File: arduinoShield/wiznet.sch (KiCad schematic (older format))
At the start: 54 parts

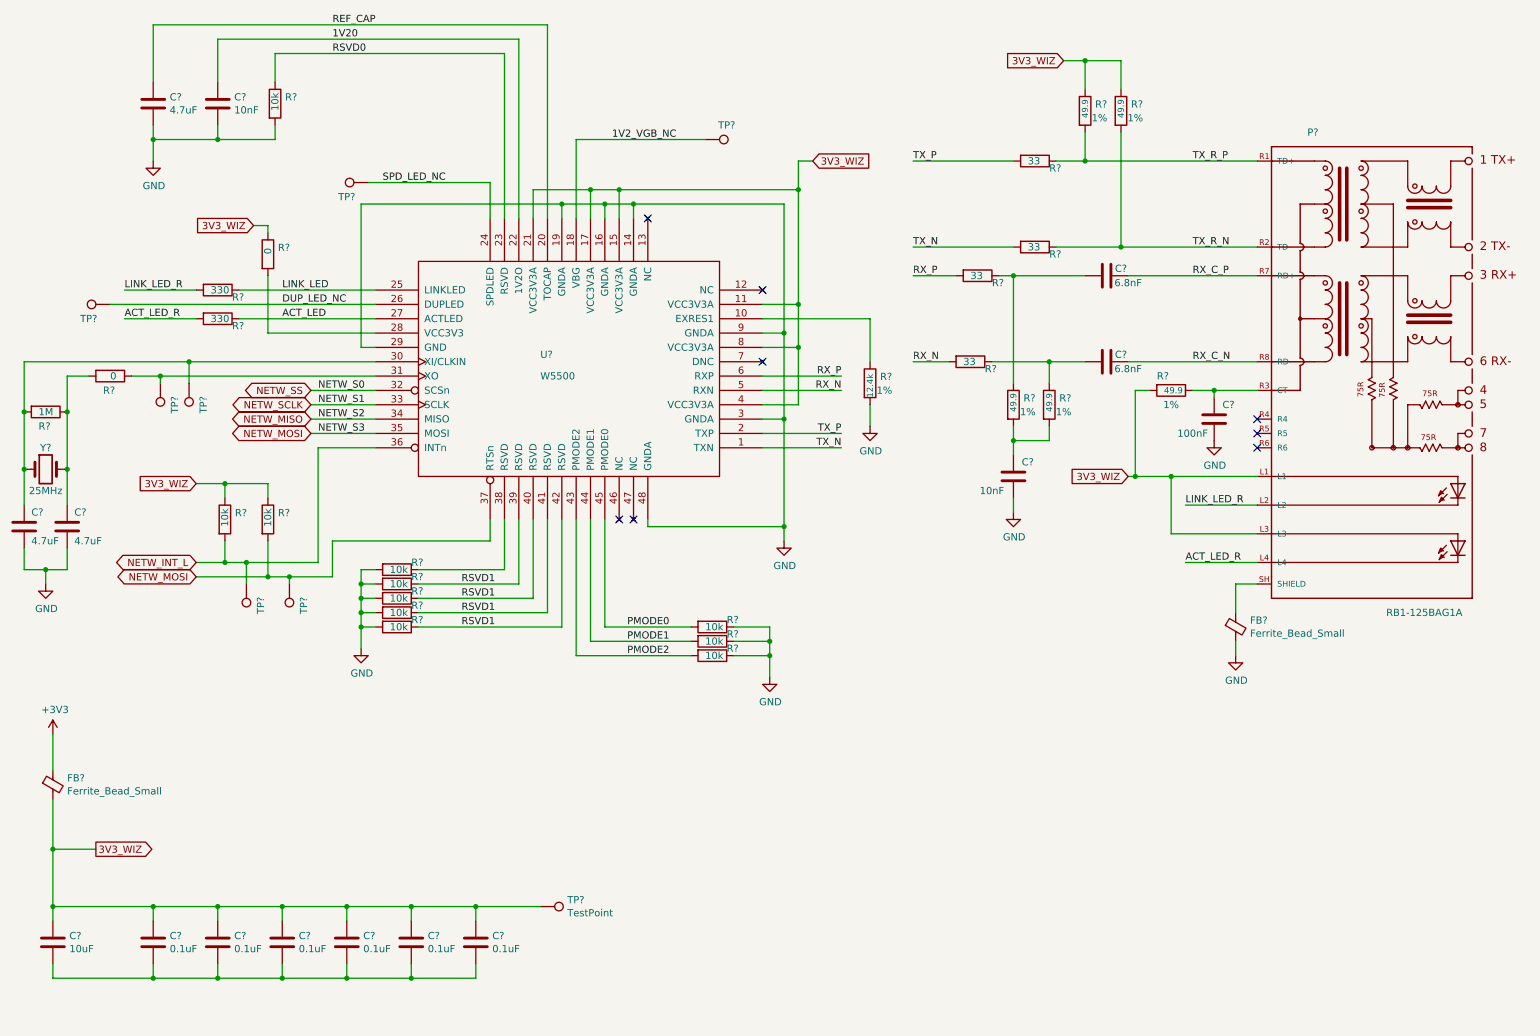
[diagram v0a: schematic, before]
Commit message: Added sensors
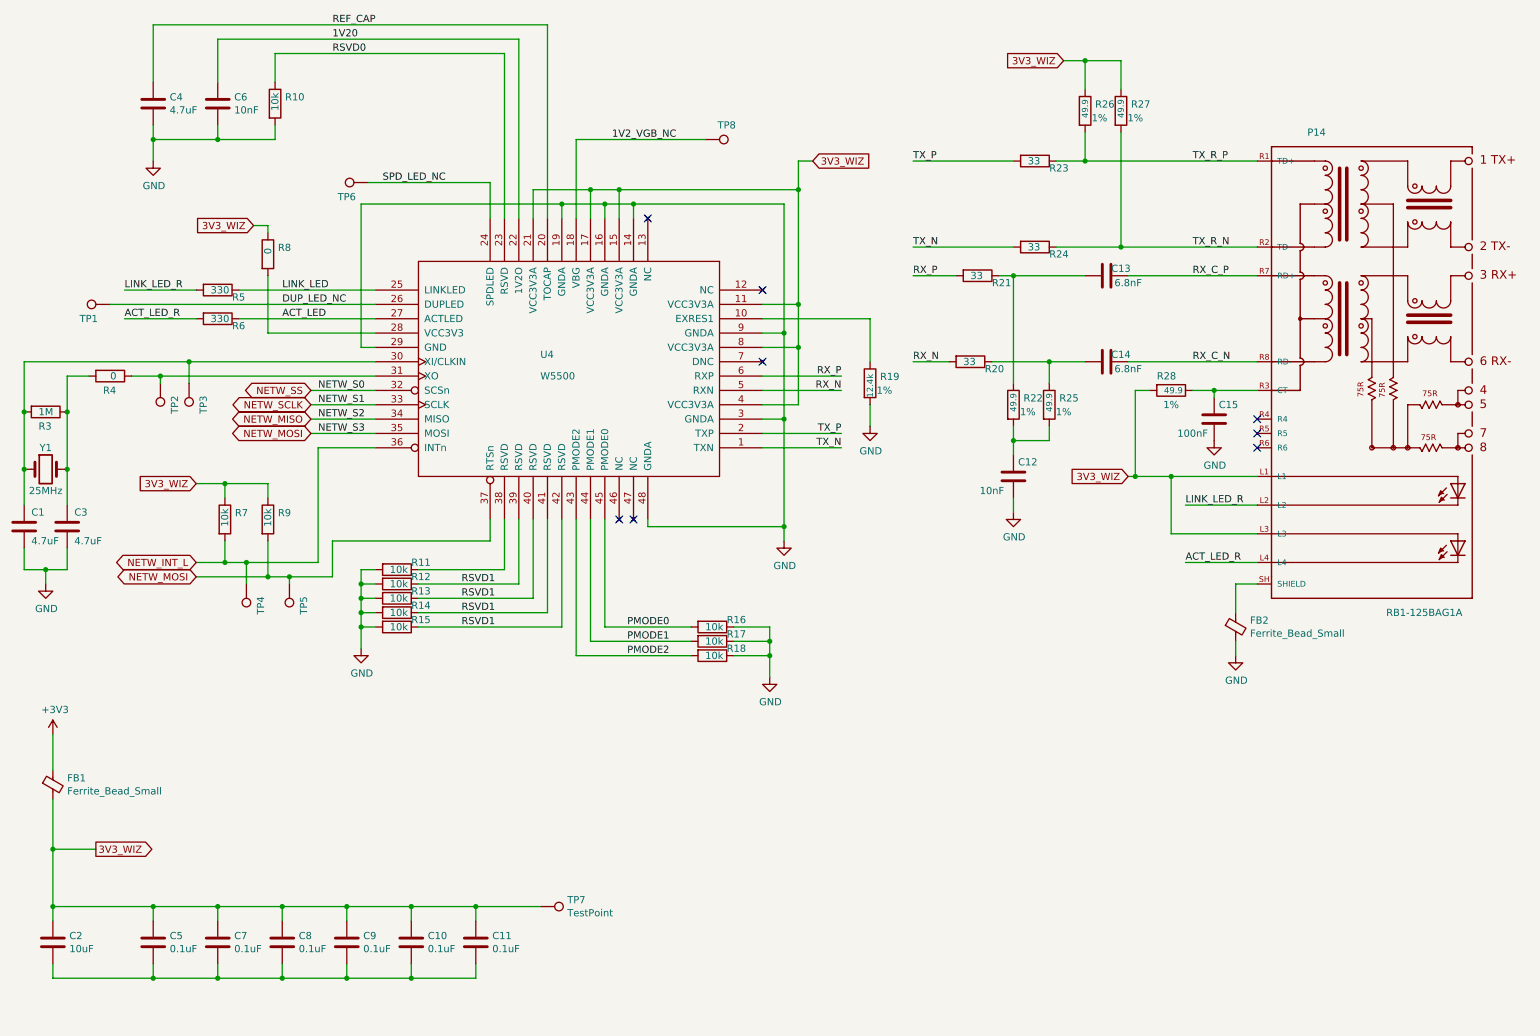
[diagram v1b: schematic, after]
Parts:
- gave numbers to parts that had none: 54

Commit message: Starting layout
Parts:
- P14: footprint WIZNET_RB1-125BAG1A -> footprints:WIZNET_RB1-125BAG1A
- U4: footprint MODULE -> footprints:QFP50P900X900X160-48N
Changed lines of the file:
@@
 F 0 "U4" H 4700 3000 50  0000 R CNN
 F 1 "W5500" H 4700 3150 50  0000 R CNN
-F 2 "MODULE" H 4500 3100 50  0001 C CNN
-F 3 "DOCUMENTATION" H 4500 3100 50  0001 C CNN
+F 2 "footprints:QFP50P900X900X160-48N" H 4500 3100 50  0001 C CNN
+F 3 "http://wizwiki.net/wiki/lib/exe/fetch.php?media=products:w5500:w5500_ds_v106e_141230.pdf" H 4500 3100 50  0001 C CNN
 	1    4500 3100
 	-1   0    0    1
@@
 F 0 "P14" H 9650 4650 50  0000 L CNN
 F 1 "RB1-125BAG1A" H 10200 1300 50  0000 L CNN
-F 2 "WIZNET_RB1-125BAG1A" H 10100 3050 50  0001 L BNN
+F 2 "footprints:WIZNET_RB1-125BAG1A" H 10100 3050 50  0001 L BNN
 F 3 "2.18 USD" H 10100 3050 50  0001 L BNN
 F 4 "Good" H 10100 3050 50  0001 L BNN "Availability"

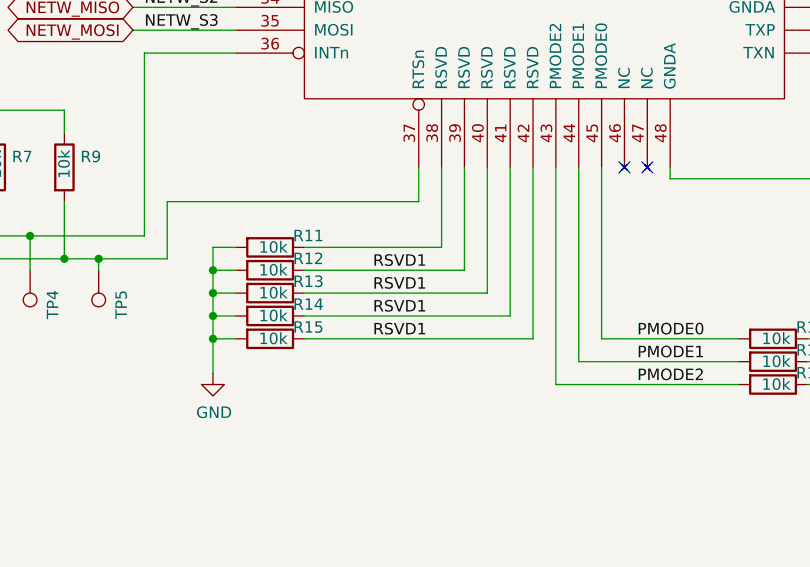
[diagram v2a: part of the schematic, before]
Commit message: Half of wiznet is layed out. Fixed PMODE termination resistors.
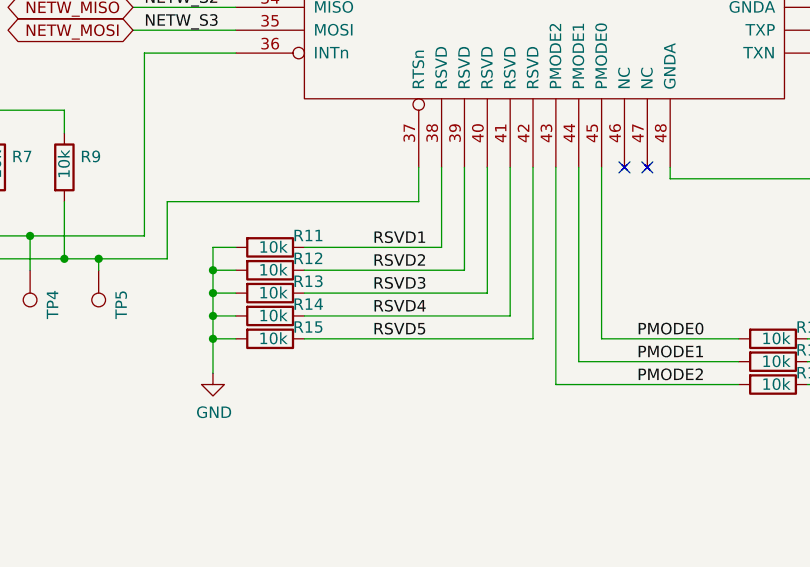
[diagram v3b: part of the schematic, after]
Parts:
- R16, R17, R18: footprint Resistors_SMD:R_0402 -> Resistors_SMD:R_0805
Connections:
- net RSVD1: now also R11.1, U4.38 (RSVD); no longer R12.1, R13.1, R14.1, R15.1, U4.39 (RSVD), U4.40 (RSVD), U4.41 (RSVD), U4.42 (RSVD)
- new net RSVD2: R12.1, U4.39 (RSVD)
- new net RSVD3: R13.1, U4.40 (RSVD)
- new net RSVD4: R14.1, U4.41 (RSVD)
- new net RSVD5: R15.1, U4.42 (RSVD)
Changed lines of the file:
@@
 Text Label 5200 4900 2    50   ~ 0
 PMODE0
+Text Label 3750 4500 0    50   ~ 0
+RSVD1
 Text Label 3750 4600 0    50   ~ 0
-RSVD1
+RSVD2
 Text Label 3750 4700 0    50   ~ 0
-RSVD1
+RSVD3
 Text Label 3750 4800 0    50   ~ 0
-RSVD1
-Text Label 3750 4900 0    50   ~ 0
-RSVD1
+RSVD4
 Wire Wire Line
 	700  3050 1850 3050
@@
 F 0 "R16" V 5450 5000 50  0000 L CNN
 F 1 "10k" V 5500 4850 50  0000 L CNN
-F 2 "Resistors_SMD:R_0402" V 5430 4900 50  0001 C CNN
+F 2 "Resistors_SMD:R_0805" V 5430 4900 50  0001 C CNN
 F 3 "~" H 5500 4900 50  0001 C CNN
 	1    5500 4900
@@
 F 0 "R17" V 5450 5100 50  0000 L CNN
 F 1 "10k" V 5500 4950 50  0000 L CNN
-F 2 "Resistors_SMD:R_0402" V 5430 5000 50  0001 C CNN
+F 2 "Resistors_SMD:R_0805" V 5430 5000 50  0001 C CNN
 F 3 "~" H 5500 5000 50  0001 C CNN
 	1    5500 5000
@@
 F 0 "R18" V 5450 5200 50  0000 L CNN
 F 1 "10k" V 5500 5050 50  0000 L CNN
-F 2 "Resistors_SMD:R_0402" V 5430 5100 50  0001 C CNN
+F 2 "Resistors_SMD:R_0805" V 5430 5100 50  0001 C CNN
 F 3 "~" H 5500 5100 50  0001 C CNN
 	1    5500 5100
@@
 Text Label 8850 3050 0    50   ~ 0
 RX_C_N
+Text Label 3750 4900 0    50   ~ 0
+RSVD5
 $EndSCHEMATC

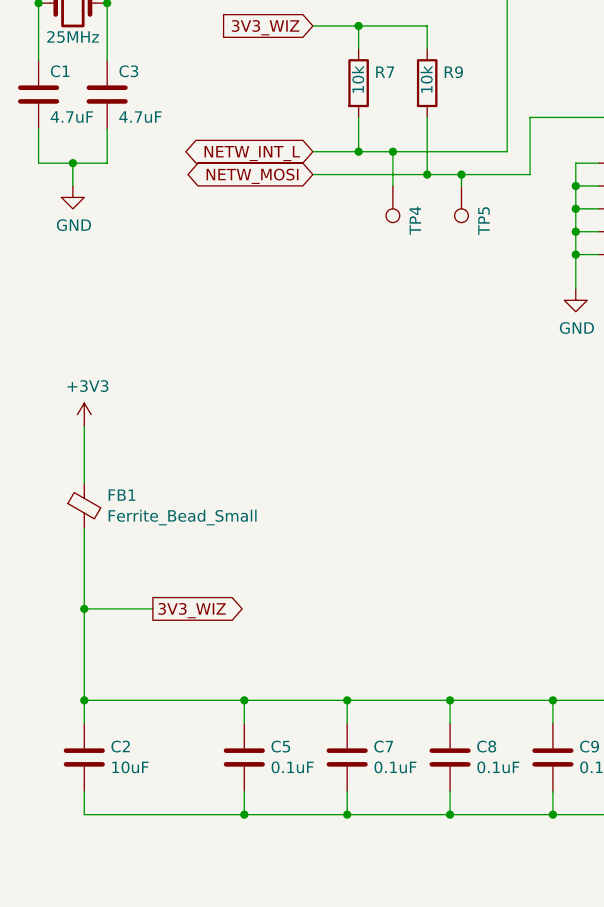
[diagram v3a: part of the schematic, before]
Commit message: Inital layout done. Starting routing. Need to add breakout headers for analogue.
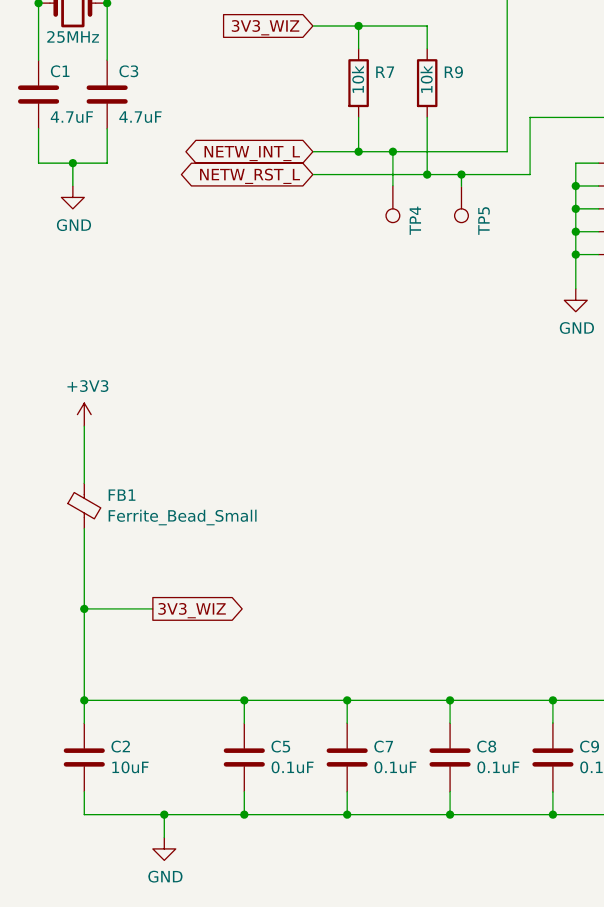
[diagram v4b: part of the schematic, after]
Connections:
- net GND: now also C10.2, C11.2, C2.2, C5.2, C7.2, C8.2, C9.2
- net NETW_MOSI: no longer R9.2, TP5.1, U4.37 (RTSn)
- new net NETW_RST_L: R9.2, TP5.1, U4.37 (RTSn)
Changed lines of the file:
@@
 	3400 7350 3850 7350
 Wire Wire Line
-	1600 7350 900  7350
+	1600 7350 1250 7350
 Wire Wire Line
 	900  7350 900  7250
@@
 NETW_INT_L
 Text GLabel 1900 4550 0    50   BiDi ~ 0
-NETW_MOSI
+NETW_RST_L
 $Comp
 L Device:R R7
@@
 Text Label 3750 4900 0    50   ~ 0
 RSVD5
+$Comp
+L power:GND #PWR?
+U 1 1 5CF3217B
+P 1250 7450
+F 0 "#PWR?" H 1250 7200 50  0001 C CNN
+F 1 "GND" H 1255 7277 50  0000 C CNN
+F 2 "" H 1250 7450 50  0001 C CNN
+F 3 "" H 1250 7450 50  0001 C CNN
+	1    1250 7450
+	1    0    0    -1
+$EndComp
+Connection ~ 1250 7350
+Wire Wire Line
+	1250 7350 900  7350
+Wire Wire Line
+	1250 7450 1250 7350
 $EndSCHEMATC

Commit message: Power planes created. Started routing.
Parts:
- FB1: footprint Resistors_SMD:R_0402 -> Resistors_SMD:R_1206
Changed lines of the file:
@@
 F 0 "FB1" H 1000 6046 50  0000 L CNN
 F 1 "Ferrite_Bead_Small" H 1000 5955 50  0000 L CNN
-F 2 "Resistors_SMD:R_0402" V 830 6000 50  0001 C CNN
+F 2 "Resistors_SMD:R_1206" V 830 6000 50  0001 C CNN
 F 3 "~" H 900 6000 50  0001 C CNN
 	1    900  6000
@@
 RSVD5
 $Comp
-L power:GND #PWR?
+L power:GND #PWR0118
 U 1 1 5CF3217B
 P 1250 7450
-F 0 "#PWR?" H 1250 7200 50  0001 C CNN
+F 0 "#PWR0118" H 1250 7200 50  0001 C CNN
 F 1 "GND" H 1255 7277 50  0000 C CNN
 F 2 "" H 1250 7450 50  0001 C CNN

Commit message: Made slack changes from review
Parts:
- added R38, R39, R40: 0, Resistors_SMD:R_0402, symbol Device:R
- P14: symbol hyper_capstone:RB1-125BAG1A -> arduinoShield-rescue:RB1-125BAG1A-hyper_capstone
- U4: symbol hyper_capstone:W5500 -> arduinoShield-rescue:W5500-hyper_capstone
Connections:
- net NETW_MOSI: now also R40.2; no longer U4.35 (MOSI)
- net NETW_SCLK: now also R39.2; no longer U4.33 (SCLK)
- net NETW_SS: now also R38.2; no longer U4.32 (SCSn)
- new net NETW_S0: R38.1, U4.32 (SCSn)
- new net NETW_S1: R39.1, U4.33 (SCLK)
- new net NETW_S3: R40.1, U4.35 (MOSI)
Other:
- moved on the sheet: TP2, TP3
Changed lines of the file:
@@
 $EndDescr
 $Comp
-L hyper_capstone:W5500 U4
+L arduinoShield-rescue:W5500-hyper_capstone U4
 U 1 1 5D492E66
 P 4500 3100
+AR Path="/5D492E66" Ref="U4"  Part="1"
+AR Path="/5D492DEA/5D492E66" Ref="U4"  Part="1"
 F 0 "U4" H 4700 3000 50  0000 R CNN
 F 1 "W5500" H 4700 3150 50  0000 R CNN
@@
 	0    1    1    0
 $EndComp
-Text GLabel 2700 3250 0    50   BiDi ~ 0
+Text GLabel 2170 3250 0    50   BiDi ~ 0
 NETW_SS
 Text Label 2750 3250 0    50   ~ 0
 NETW_S0
-Wire Wire Line
-	2700 3250 3150 3250
-Text GLabel 2700 3350 0    50   BiDi ~ 0
+Text GLabel 2170 3350 0    50   BiDi ~ 0
 NETW_SCLK
 Text Label 2750 3350 0    50   ~ 0
 NETW_S1
-Wire Wire Line
-	2700 3350 3150 3350
-Text GLabel 2700 3450 0    50   BiDi ~ 0
+Text GLabel 2170 3450 0    50   BiDi ~ 0
 NETW_MISO
 Text Label 2750 3450 0    50   ~ 0
 NETW_S2
-Wire Wire Line
-	2700 3450 3150 3450
-Text GLabel 2700 3550 0    50   BiDi ~ 0
+Text GLabel 2170 3550 0    50   BiDi ~ 0
 NETW_MOSI
 Text Label 2750 3550 0    50   ~ 0
 NETW_S3
-Wire Wire Line
-	2700 3550 3150 3550
 $Comp
 L Connector:TestPoint TP3
 U 1 1 5D524E62
-P 1850 3200
-F 0 "TP3" V 1750 3350 50  0000 C CNN
-F 1 " " V 1954 3274 50  0000 C CNN
-F 2 "Measurement_Points:Measurement_Point_Round-SMD-Pad_Small" H 2050 3200 50  0001 C CNN
-F 3 "~" H 2050 3200 50  0001 C CNN
-	1    1850 3200
+P 1620 3220
+F 0 "TP3" V 1620 3470 50  0000 C CNN
+F 1 " " V 1724 3294 50  0000 C CNN
+F 2 "Measurement_Points:Measurement_Point_Round-SMD-Pad_Small" H 1820 3220 50  0001 C CNN
+F 3 "~" H 1820 3220 50  0001 C CNN
+	1    1620 3220
 	-1   0    0    1
 $EndComp
@@
 L Connector:TestPoint TP2
 U 1 1 5D524F1D
-P 1650 3200
-F 0 "TP2" V 1550 3350 50  0000 C CNN
-F 1 " " V 1754 3274 50  0000 C CNN
-F 2 "Measurement_Points:Measurement_Point_Round-SMD-Pad_Small" H 1850 3200 50  0001 C CNN
-F 3 "~" H 1850 3200 50  0001 C CNN
-	1    1650 3200
+P 1450 3210
+F 0 "TP2" V 1430 3470 50  0000 C CNN
+F 1 " " V 1554 3284 50  0000 C CNN
+F 2 "Measurement_Points:Measurement_Point_Round-SMD-Pad_Small" H 1650 3210 50  0001 C CNN
+F 3 "~" H 1650 3210 50  0001 C CNN
+	1    1450 3210
 	-1   0    0    1
 $EndComp
 Wire Wire Line
-	1850 3200 1850 3050
-Wire Wire Line
-	1650 3200 1650 3150
+	1620 3220 1850 3050
+Wire Wire Line
+	1450 3210 1650 3150
 Connection ~ 1650 3150
 Wire Wire Line
@@
 $EndBitmap
 $Comp
-L hyper_capstone:RB1-125BAG1A P14
+L arduinoShield-rescue:RB1-125BAG1A-hyper_capstone P14
 U 1 1 5D7A0B8B
 P 10100 3050
+AR Path="/5D7A0B8B" Ref="P14"  Part="1"
+AR Path="/5D492DEA/5D7A0B8B" Ref="P14"  Part="1"
 F 0 "P14" H 9650 4650 50  0000 L CNN
 F 1 "RB1-125BAG1A" H 10200 1300 50  0000 L CNN
@@
 Wire Wire Line
 	1250 7450 1250 7350
+$Comp
+L Device:R R38
+U 1 1 5D0E7532
+P 2320 3250
+F 0 "R38" V 2320 3250 50  0000 L CNN
+F 1 "0" V 2320 3200 50  0000 L CNN
+F 2 "Resistors_SMD:R_0402" V 2250 3250 50  0001 C CNN
+F 3 "~" H 2320 3250 50  0001 C CNN
+	1    2320 3250
+	0    1    1    0
+$EndComp
+$Comp
+L Device:R R39
+U 1 1 5D0E785D
+P 2320 3350
+F 0 "R39" V 2320 3350 50  0000 L CNN
+F 1 "0" V 2320 3300 50  0000 L CNN
+F 2 "Resistors_SMD:R_0402" V 2250 3350 50  0001 C CNN
+F 3 "~" H 2320 3350 50  0001 C CNN
+	1    2320 3350
+	0    1    1    0
+$EndComp
+$Comp
+L Device:R R40
+U 1 1 5D0E798B
+P 2320 3550
+F 0 "R40" V 2320 3550 50  0000 L CNN
+F 1 "0" V 2320 3500 50  0000 L CNN
+F 2 "Resistors_SMD:R_0402" V 2250 3550 50  0001 C CNN
+F 3 "~" H 2320 3550 50  0001 C CNN
+	1    2320 3550
+	0    1    1    0
+$EndComp
+Wire Wire Line
+	2470 3550 3150 3550
+Wire Wire Line
+	2470 3350 3150 3350
+Wire Wire Line
+	2470 3250 3150 3250
+Wire Wire Line
+	2170 3450 3150 3450
 $EndSCHEMATC
